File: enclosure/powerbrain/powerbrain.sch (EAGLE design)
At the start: 38 parts, among them J2 USB-A-S, J3 AVR_SPI_PRG_6PTH, Q1 FDD4141TO252, Q2 200mA/50V, U1 TPS61090, X2 ZX62D-B-5PA8

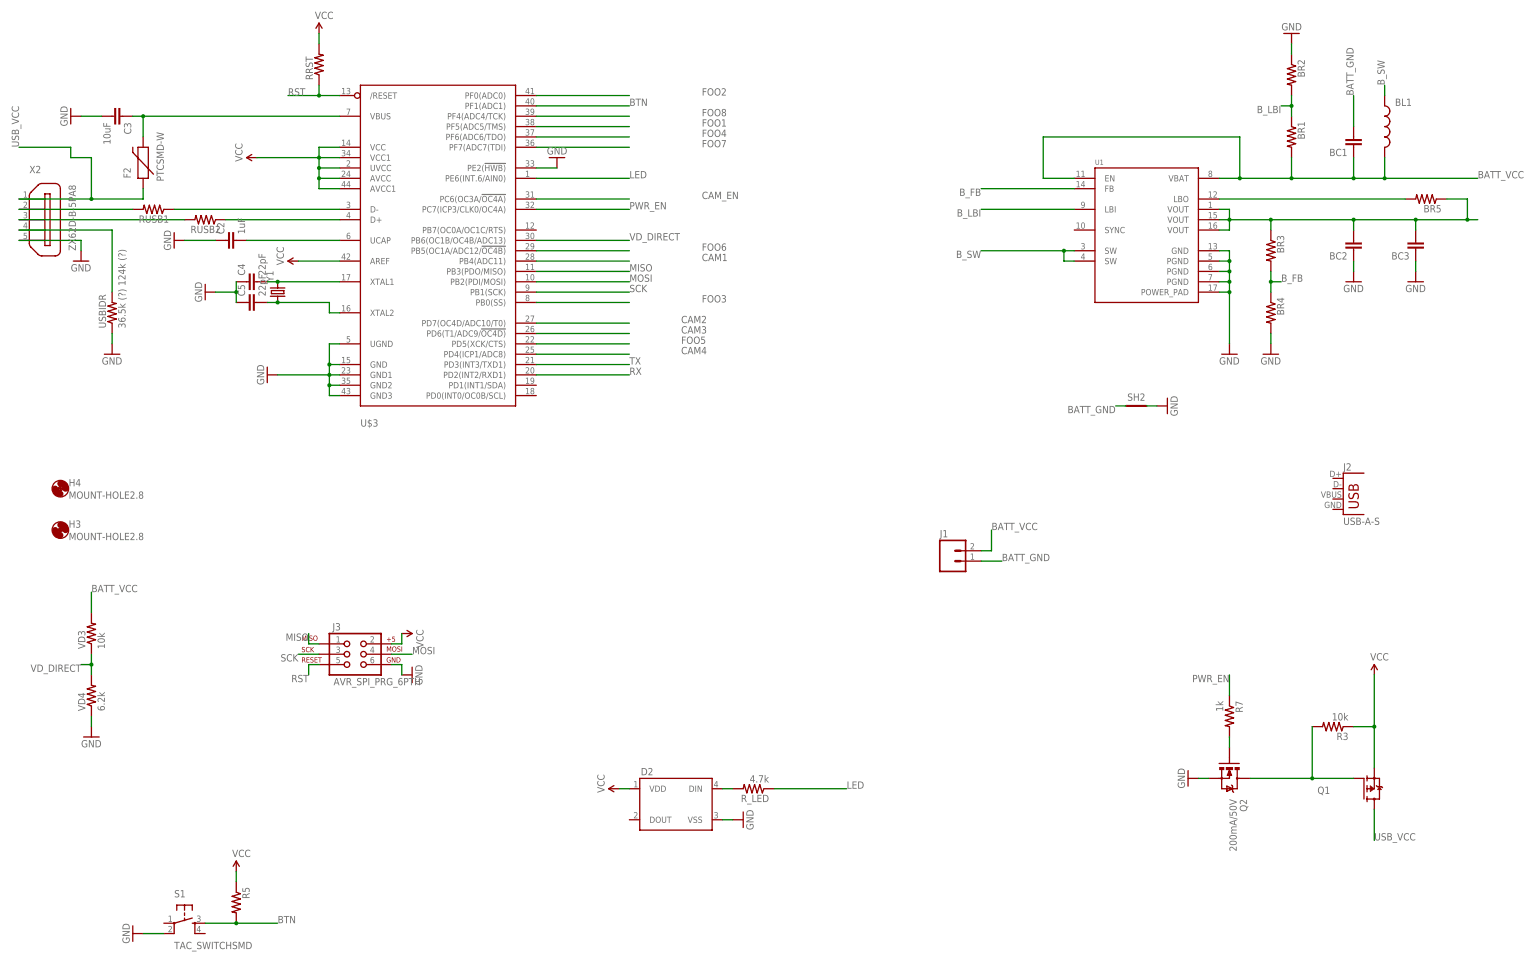
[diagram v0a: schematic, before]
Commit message: powerbrain: routing improved
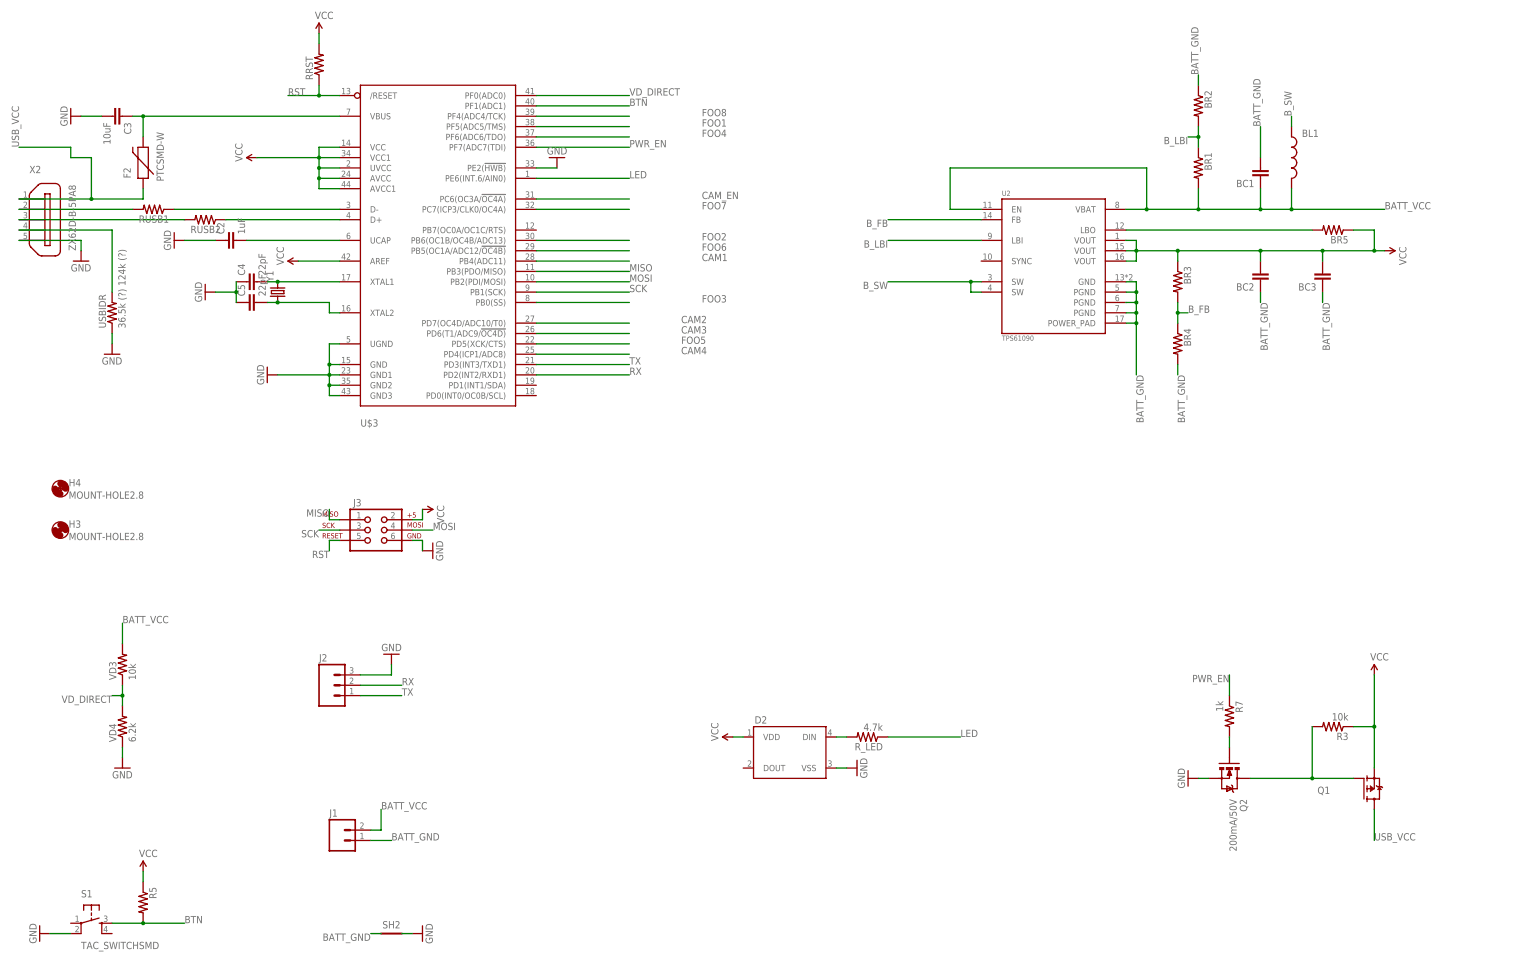
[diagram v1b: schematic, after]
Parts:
- removed U1: TPS61090, TPS61090:TPS61090
- added U2: TPS61090, TPS61090:TPS61090
- J2: value USB-A-S -> (none); device SparkFun-Connectors:USB-A-S -> SparkFun-Connectors:M03PTH
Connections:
- removed net N$15: BC2.2, BC3.2, BR3.1, BR5.1, U1.VOUT@1, U1.VOUT@2, U1.VOUT@3
- net BATT_GND: now also BC2.1, BC3.1, BR2.1, BR4.2, U2.GND, U2.PGND@1, U2.PGND@2, U2.PGND@3, U2.POWER_PAD
- net BATT_VCC: now also U2.EN, U2.VBAT; no longer U1.EN, U1.VBAT
- net B_FB: now also U2.FB; no longer U1.FB
- net B_LBI: now also U2.LBI; no longer U1.LBI
- net B_SW: now also U2.SW@1, U2.SW@2; no longer U1.SW@1, U1.SW@2
- net FOO2: now also U$3.PB6(OC1B/OC4B/ADC13); no longer U$3.PF0(ADC0)
- net FOO7: now also U$3.PC7(ICP3/CLK0/OC4A); no longer U$3.PF7(ADC7(TDI)
- net GND: now also J2.3; no longer BC2.1, BC3.1, BR2.1, BR4.2, U1.GND, U1.PGND@1, U1.PGND@2, U1.PGND@3, U1.POWER_PAD
- net N$16: now also U2.LBO; no longer U1.LBO
- net PWR_EN: now also U$3.PF7(ADC7(TDI); no longer U$3.PC7(ICP3/CLK0/OC4A)
- net RX: now also J2.2
- net TX: now also J2.1
- net VCC: now also BC2.2, BC3.2, BR3.1, BR5.1, U2.VOUT@1, U2.VOUT@2, U2.VOUT@3
- net VD_DIRECT: now also U$3.PF0(ADC0); no longer U$3.PB6(OC1B/OC4B/ADC13)
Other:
- moved on the sheet: BC1, BC2, BC3, BL1, BR1, BR2, BR3, BR4, BR5, D2, J1, J3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

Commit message: powerbrain: layout improved
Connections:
- net BATT_GND: now also U2.SYNC
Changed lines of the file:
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@@
 <part name="J3" library="SparkFun-Connectors" deviceset="AVR_SPI_PRG_6" device="PTH" value=""/>
 <part name="GND4" library="SparkFun-Aesthetics" deviceset="GND" device=""/>
-<part name="U2" library="TPS61090" deviceset="TPS61090" device=""/>
+<part name="U2" library="TPS61090" deviceset="TPS61090" device="" value=""/>
 <part name="SUPPLY7" library="SparkFun-Aesthetics" deviceset="VCC" device=""/>
 <part name="J2" library="SparkFun-Connectors" deviceset="M03" device="PTH"/>
@@
 <label x="302.26" y="231.14" size="1.778" layer="95" rot="R90"/>
 </segment>
-</net>
+<segment>
+<pinref part="U2" gate="G$1" pin="SYNC"/>
+<wire x1="248.92" y1="185.42" x2="238.76" y2="185.42" width="0.1524" layer="91"/>
+<label x="238.76" y="185.42" size="1.778" layer="95" rot="R180"/>
+</segment>
+</net>

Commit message: powerbrain: layout improved
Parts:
- added J4: (no value), SparkFun-Connectors:M02LOCK
- renumbered VD3 to VD1, VD4 to VD2
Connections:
- net BATT_GND: now also J4.1
- net BATT_VCC: now also J4.2
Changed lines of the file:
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@@
 <?xml version="1.0" encoding="utf-8"?>
 <!DOCTYPE eagle SYSTEM "eagle.dtd">
-<eagle version="8.2.1">
+<eagle version="8.2.2">
 <drawing>
 <settings>
@@
 <part name="FRAME4" library="SparkFun-Retired" deviceset="FRAME-A3" device=""/>
 <part name="F2" library="SparkFun-PowerIC" deviceset="PTC" device="SMD-W"/>
-<part name="VD3" library="SparkFun-Passives" deviceset="RESISTOR" device="1206" value="10k"/>
-<part name="VD4" library="SparkFun-Passives" deviceset="RESISTOR" device="1206" value="6.2k"/>
+<part name="VD1" library="SparkFun-Passives" deviceset="RESISTOR" device="1206" value="10k"/>
+<part name="VD2" library="SparkFun-Passives" deviceset="RESISTOR" device="1206" value="6.2k"/>
 <part name="J1" library="SparkFun-Connectors" deviceset="M02" device="LOCK"/>
 <part name="BL1" library="SparkFun-Passives" deviceset="INDUCTOR" device="NPI75"/>
@@
 <part name="SUPPLY7" library="SparkFun-Aesthetics" deviceset="VCC" device=""/>
 <part name="J2" library="SparkFun-Connectors" deviceset="M03" device="PTH"/>
+<part name="J4" library="SparkFun-Connectors" deviceset="M02" device="LOCK"/>
 </parts>
 <sheets>
@@
 <instance part="FRAME4" gate="G$1" x="0" y="0"/>
 <instance part="F2" gate="G$1" x="43.18" y="208.28" rot="R90"/>
-<instance part="VD3" gate="G$1" x="38.1" y="86.36" rot="R90"/>
-<instance part="VD4" gate="G$1" x="38.1" y="71.12" rot="R90"/>
+<instance part="VD1" gate="G$1" x="38.1" y="86.36" rot="R90"/>
+<instance part="VD2" gate="G$1" x="38.1" y="71.12" rot="R90"/>
 <instance part="J1" gate="G$1" x="91.44" y="43.18"/>
 <instance part="BL1" gate="G$1" x="325.12" y="210.82"/>
@@
 <instance part="SUPPLY7" gate="G$1" x="347.98" y="187.96" rot="R270"/>
 <instance part="J2" gate="J$1" x="88.9" y="81.28"/>
+<instance part="J4" gate="G$1" x="78.74" y="43.18"/>
 </instances>
 <busses>
@@
 </segment>
 <segment>
-<pinref part="VD4" gate="G$1" pin="1"/>
+<pinref part="VD2" gate="G$1" pin="1"/>
 <wire x1="38.1" y1="66.04" x2="38.1" y2="63.5" width="0.1524" layer="91"/>
 <pinref part="GND6" gate="1" pin="GND"/>
@@
 <net name="VD_DIRECT" class="0">
 <segment>
-<pinref part="VD3" gate="G$1" pin="1"/>
-<pinref part="VD4" gate="G$1" pin="2"/>
+<pinref part="VD1" gate="G$1" pin="1"/>
+<pinref part="VD2" gate="G$1" pin="2"/>
 <wire x1="38.1" y1="81.28" x2="38.1" y2="78.74" width="0.1524" layer="91"/>
 <wire x1="38.1" y1="78.74" x2="38.1" y2="76.2" width="0.1524" layer="91"/>
@@
 <net name="BATT_VCC" class="2">
 <segment>
-<pinref part="VD3" gate="G$1" pin="2"/>
+<pinref part="VD1" gate="G$1" pin="2"/>
 <wire x1="38.1" y1="91.44" x2="38.1" y2="96.52" width="0.1524" layer="91"/>
 <label x="38.1" y="96.52" size="1.778" layer="95"/>
@@
 <label x="101.6" y="50.8" size="1.778" layer="95"/>
 <pinref part="J1" gate="G$1" pin="2"/>
+<pinref part="J4" gate="G$1" pin="2"/>
+<wire x1="86.36" y1="45.72" x2="99.06" y2="45.72" width="0.1524" layer="91"/>
+<junction x="99.06" y="45.72"/>
 </segment>
 <segment>
@@
 <pinref part="J1" gate="G$1" pin="1"/>
 <label x="104.14" y="43.18" size="1.778" layer="95"/>
-</segment>
-<segment>
+<pinref part="J4" gate="G$1" pin="1"/>
+<wire x1="99.06" y1="43.18" x2="86.36" y2="43.18" width="0.1524" layer="91"/>
+<junction x="99.06" y="43.18"/>
+</segment>
+<segment>

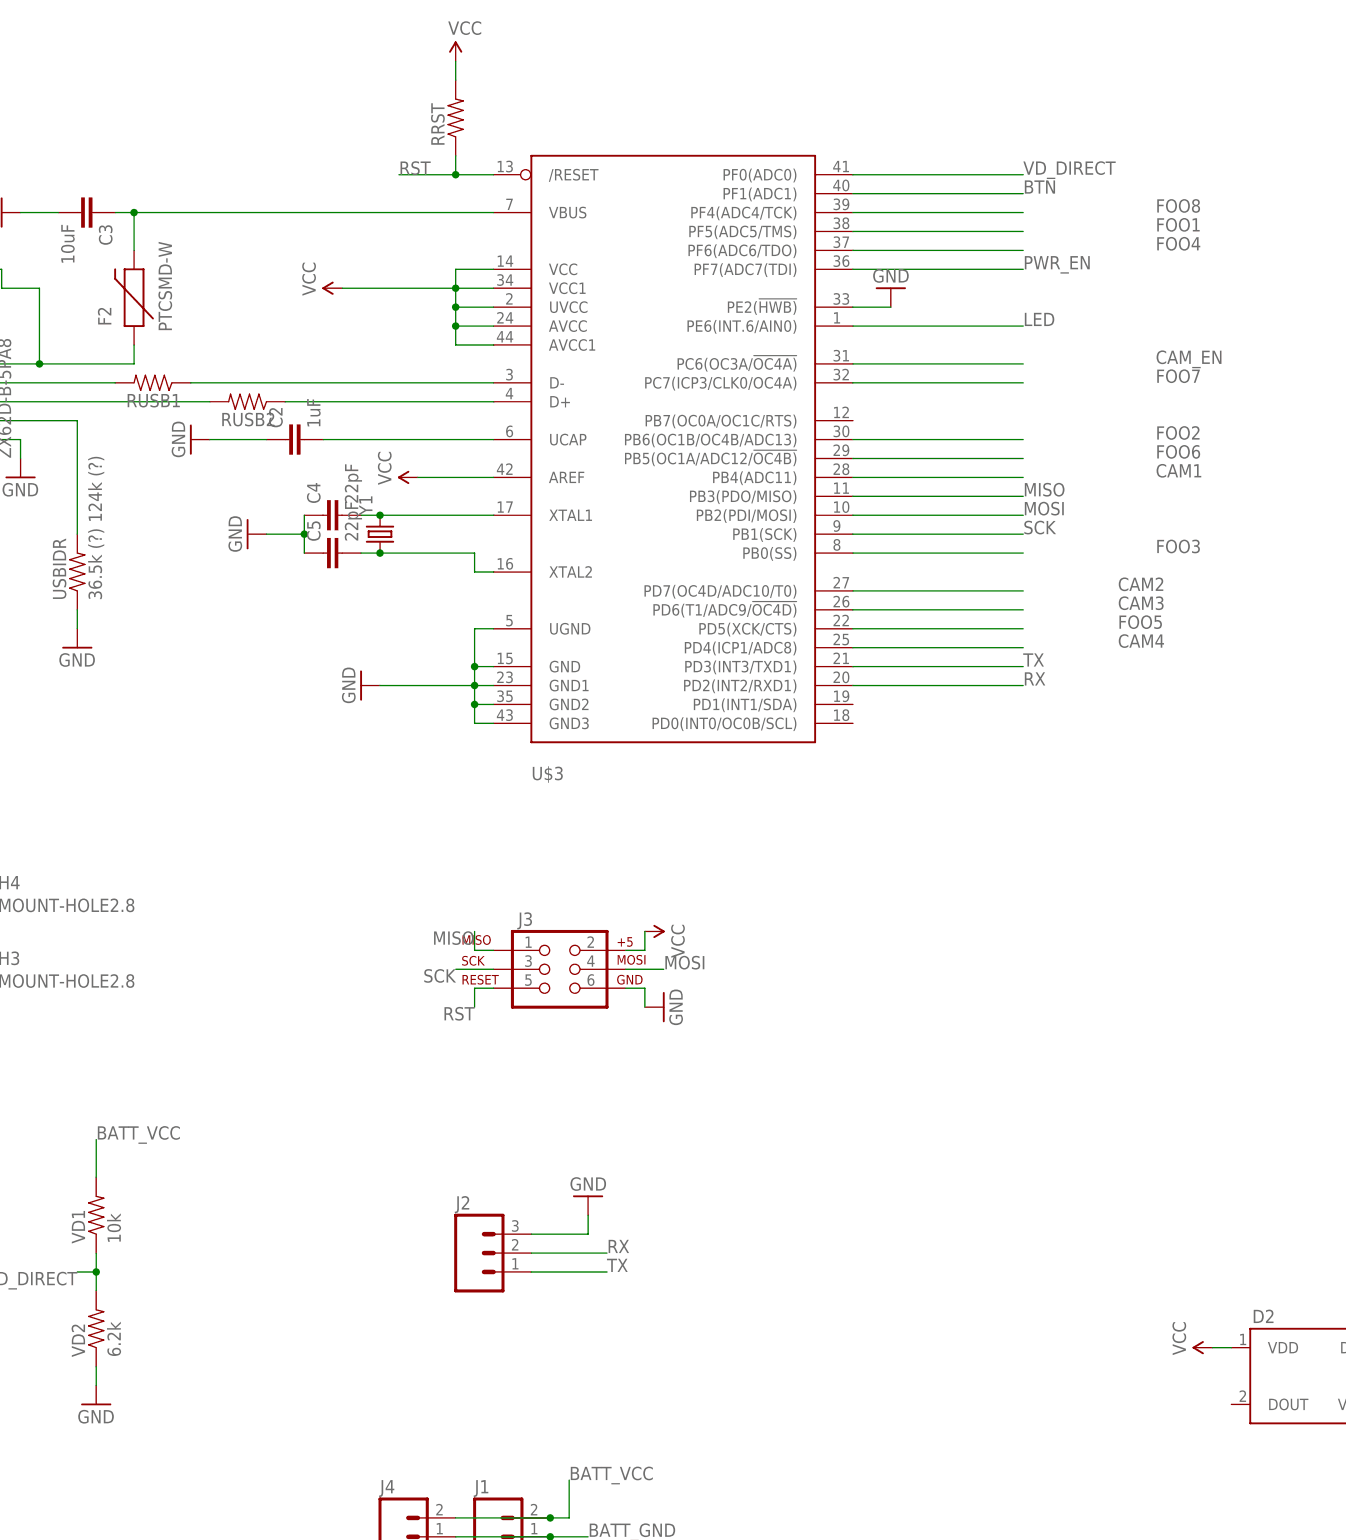
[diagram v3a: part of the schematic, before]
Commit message: powerbrain: USB OTG vbus unclear
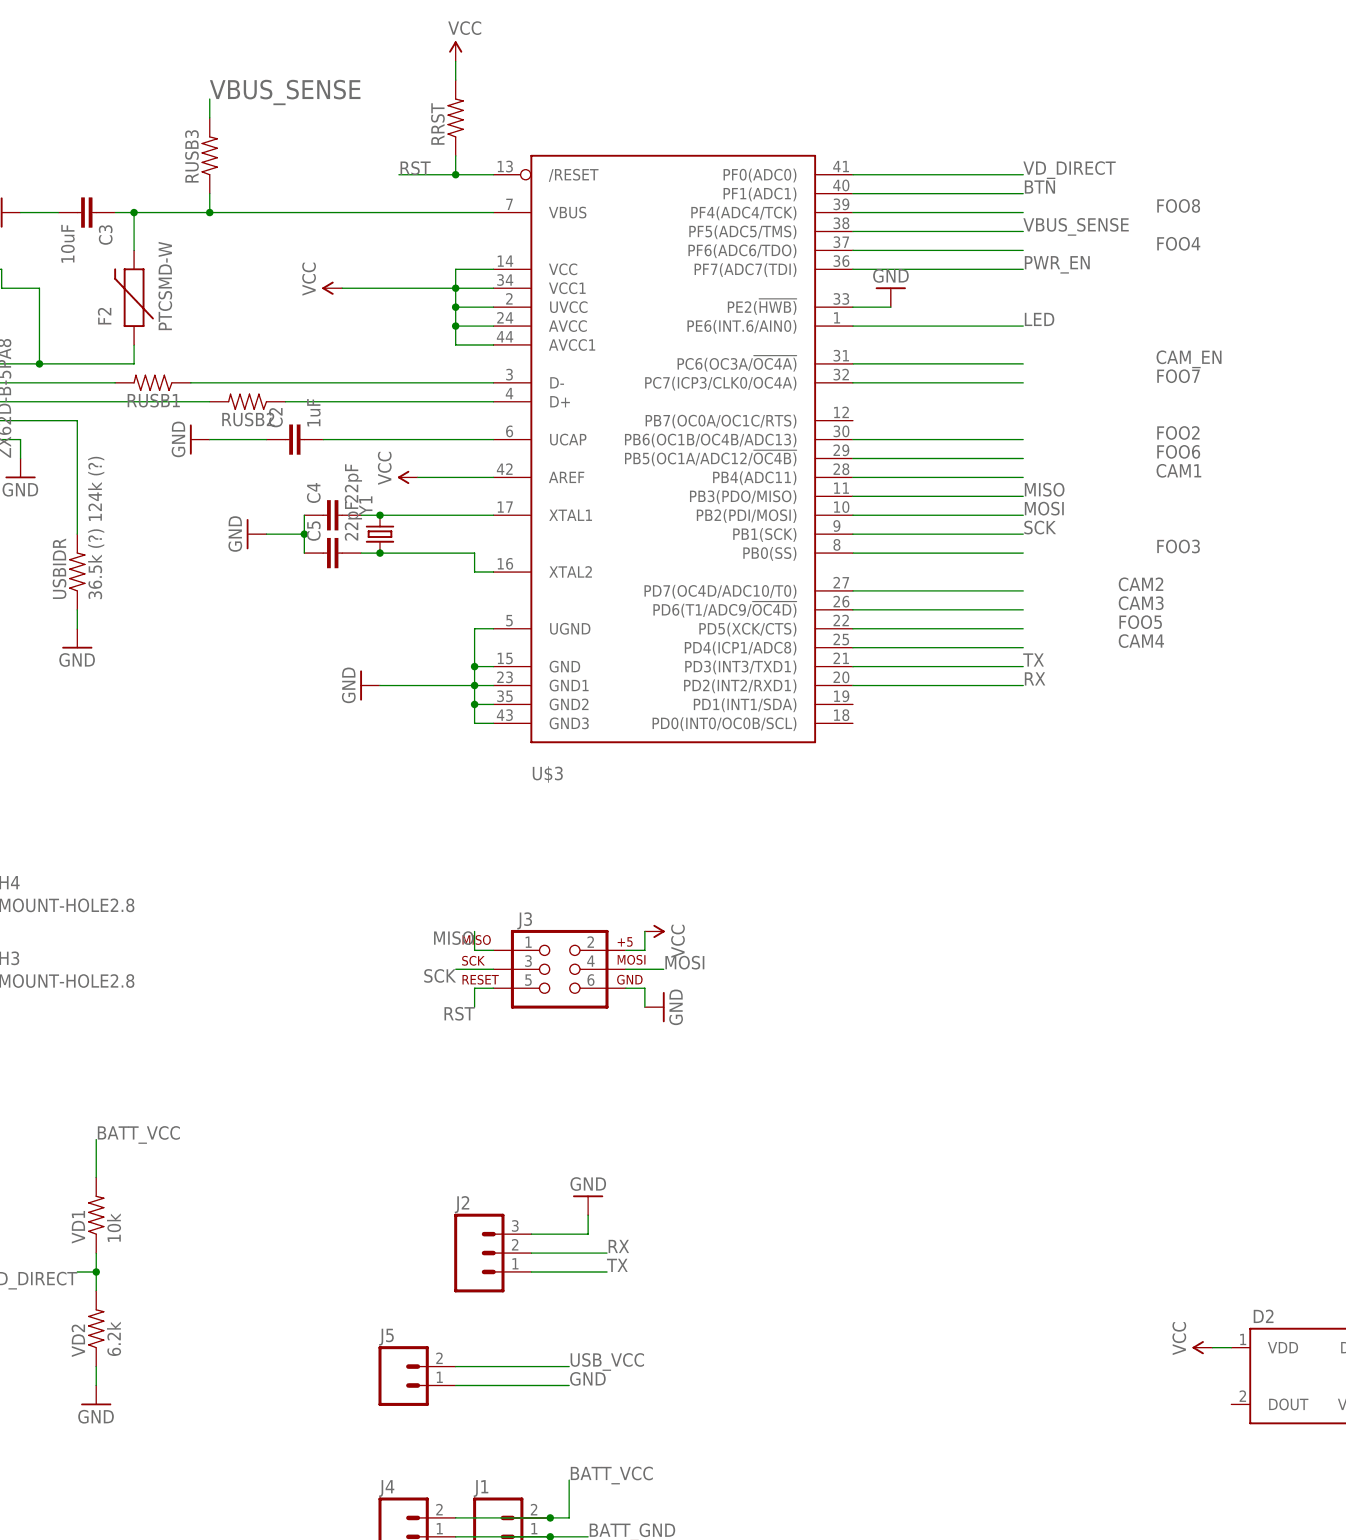
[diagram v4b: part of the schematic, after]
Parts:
- added J5: (no value), SparkFun-Connectors:M02LOCK
- added RUSB3: (no value), SparkFun-Passives:RESISTOR1206
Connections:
- removed net FOO1: U$3.PF5(ADC5/TMS)
- removed net N$22: C3.1, F2.2, U$3.VBUS
- new net $N23: C3.1, F2.2, RUSB3.1, U$3.VBUS
- new net VBUS_SENSE: RUSB3.2, U$3.PF5(ADC5/TMS)
- net GND: now also J5.1
- net USB_VCC: now also J5.2
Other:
- note added: "?"
